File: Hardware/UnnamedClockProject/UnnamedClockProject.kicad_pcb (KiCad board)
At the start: 2 copper layers, 77.9 x 33.9 mm, 27 parts, among them J101 CLOCK_OUT, J102 POWER, Q101 2N3904, U104 G3MB-202P, U105 G3MB-202P, U106 G3MB-202P, U107 CAT24C256

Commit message: Got some work done on pcb
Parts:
- added C101: 100nF, Capacitor_THT:C_Disc_D5.0mm_W2.5mm_P5.00mm, F.Cu at (-18.0, -1.50)
- added D101: STAT_LED, LED_THT:LED_D5.0mm, F.Cu at (33.0, 5.72)
- added D102: PWR, LED_THT:LED_D5.0mm, F.Cu at (26.0, 5.75)
- added R112: 1k, Resistor_THT:R_Axial_DIN0207_L6.3mm_D2.5mm_P10.16mm_Horizontal, F.Cu at (43.5, 22.6)
- added R113: 1k, Resistor_THT:R_Axial_DIN0207_L6.3mm_D2.5mm_P10.16mm_Horizontal, F.Cu at (40.0, 22.6)
- added REF**: OSHW-Logo2_14.6x12mm_SilkScreen, Symbol:OSHW-Logo2_14.6x12mm_SilkScreen, F.Cu at (-80.0, -27.0)
- added REF**: KiCad-Logo2_12mm_SilkScreen, Symbol:KiCad-Logo2_12mm_SilkScreen, B.Cu at (7.00, 50.0)
- added REF**: OSHW-Logo2_14.6x12mm_SilkScreen, Symbol:OSHW-Logo2_14.6x12mm_SilkScreen, B.Cu at (8.00, 36.0)
- RV101: footprint Potentiometer_THT:Potentiometer_Bourns_3339S_Horizontal -> Potentiometer_THT:Potentiometer_Runtron_RM-065_Vertical
- U108: moved to B.Cu
- moved RV101 374.8 mm to (-16.5, -15.8), turned to 180 degrees
- moved U107 363.7 mm to (-21.5, -8.50), turned to -90 degrees
- moved U103 335.5 mm to (-18.0, 37.0), turned to -90 degrees
- moved R111 329.1 mm to (-50.0, -30.0)
- moved Q101 306.2 mm to (34.5, 41.5), turned to 90 degrees
- moved R102 284.1 mm to (-37.7, 33.0)
- moved R101 282.8 mm to (-37.7, 36.5)
- moved D106 250.2 mm to (47.0, 5.72), turned to -90 degrees
- moved D105 237.7 mm to (54.0, 5.72), turned to -90 degrees
- moved D103 236.8 mm to (40.0, 5.72), turned to -90 degrees
- moved U104 233.3 mm to (38.4, 27.3)
- moved J102 232.7 mm to (30.9, 50.5)
- moved R105 231.1 mm to (19.5, 34.0)
- moved R104 231.0 mm to (19.4, 30.5)
- moved U106 229.5 mm to (43.4, 39.3)
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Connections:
- A101 pad 28: unconnected-(A101-D13-Pad28) -> /STAT
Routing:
- net /24VAC_L: track 0.00 -> 41.8 mm
- net /L1_OUT: track 0.00 -> 20.0 mm
- net Net-(U104-Pad14): track 0.00 -> 12.0 mm
- net /L2_OUT: track 0.00 -> 11.9 mm
- net /24VAC_N: track 0.00 -> 10.6 mm
- added copper zone on B.Cu, net GND
- added copper zone on F.Cu, net GND
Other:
- board size 77.9 x 33.9 mm -> 160 x 102 mm
- board text added: "!DIR"
- board text added: "24N"
- board text added: "24VAC"
- board text added: "CLOCK_OUT"
- board text added: "CONTRAST"
- board text added: "DIR"
- board text added: "FIX"
- board text added: "L1"
- board text added: "L2"
- board text added: "MOVE"
- board text added: "POWER"
- board text added: "PWR"
- board text added: "STAT"

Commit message: Knock out a little more before class
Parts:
- added J103: BUTTONS, Connector_JST:JST_EH_B6B-EH-A_1x06_P2.50mm_Vertical, F.Cu at (18.5, 19.0)
- moved U103 11.5 mm to (-18.0, 48.5)
- moved R101 11.0 mm to (-37.6, 47.5)
- moved R102 11.0 mm to (-37.6, 44.0)
- moved REF** 3.75 mm to (10.0, 47.8)
- moved REF** 2.06 mm to (10.0, 35.5)
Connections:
- A101 pad 10: unconnected-(A101-A1-Pad10) -> /DN_BTN
- A101 pad 11: unconnected-(A101-A2-Pad11) -> /LF_BTN
- A101 pad 12: unconnected-(A101-A3-Pad12) -> /RI_BTN
- A101 pad 15: unconnected-(A101-D0/RX-Pad15) -> /MENU_BTN
- A101 pad 9: unconnected-(A101-A0-Pad9) -> /UP_BTN
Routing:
- net +5V: track 0.00 -> 268.6 mm
- net /REG_SEL: track 0.00 -> 101.1 mm
- net /LCD_EN: track 0.00 -> 99.0 mm
- net /LCD_7: track 0.00 -> 88.9 mm
- net /LCD_6: track 0.00 -> 88.9 mm
- net /LCD_5: track 0.00 -> 88.9 mm
- net /LCD_4: track 0.00 -> 88.9 mm
- net /DIR: track 0.00 -> 42.8 mm
- net /NOT_DIR: track 0.00 -> 41.1 mm
- net /EN: track 0.00 -> 36.6 mm
- net Net-(U108-CONTRAST): track 0.00 -> 17.8 mm
- net Net-(D102-A): track 0.00 -> 15.7 mm
- net Net-(R105-Pad2): track 0.00 -> 15.2 mm
- net Net-(D101-A): track 0.00 -> 12.2 mm
- net Net-(R104-Pad2): track 0.00 -> 10.1 mm
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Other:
- outline, holes or cut-outs redrawn

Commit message: Complete mounting
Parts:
- moved U103 2.75 mm to (-18.0, 45.8)
- moved U107 1.77 mm to (-21.7, -10.2)
- moved C101 1.35 mm to (-18.5, -2.75)
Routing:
- net /STAT: track 0.00 -> 146.4 mm
- net /RI_BTN: track 0.00 -> 122.9 mm, vias 0 -> 2
- net /SDA: track 0.00 -> 120.5 mm, vias 0 -> 2
- net /SCL: track 0.00 -> 118.6 mm, vias 0 -> 2
- net /DIR: track 42.8 -> 153.8 mm, vias 0 -> 3
- net /EN: track 36.6 -> 145.5 mm, vias 0 -> 3
- net /MENU_BTN: track 0.00 -> 103.7 mm, vias 0 -> 3
- net /GPS_TX: track 0.00 -> 102.7 mm, vias 0 -> 2
- net /GPS_RX: track 0.00 -> 97.0 mm, vias 0 -> 4
- net Net-(U102-FIX): track 0.00 -> 74.1 mm
- net /GPS_PPS: track 0.00 -> 68.7 mm, vias 0 -> 3
- net /UP_BTN: track 0.00 -> 62.7 mm
- net /DN_BTN: track 0.00 -> 60.6 mm
- net /LF_BTN: track 0.00 -> 58.4 mm
- net /LCD_EN: track 99.0 -> 147.6 mm, vias 0 -> 1
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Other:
- board text added: "Unnamed Clock Project AC1JA ${FULL_REVISION}"

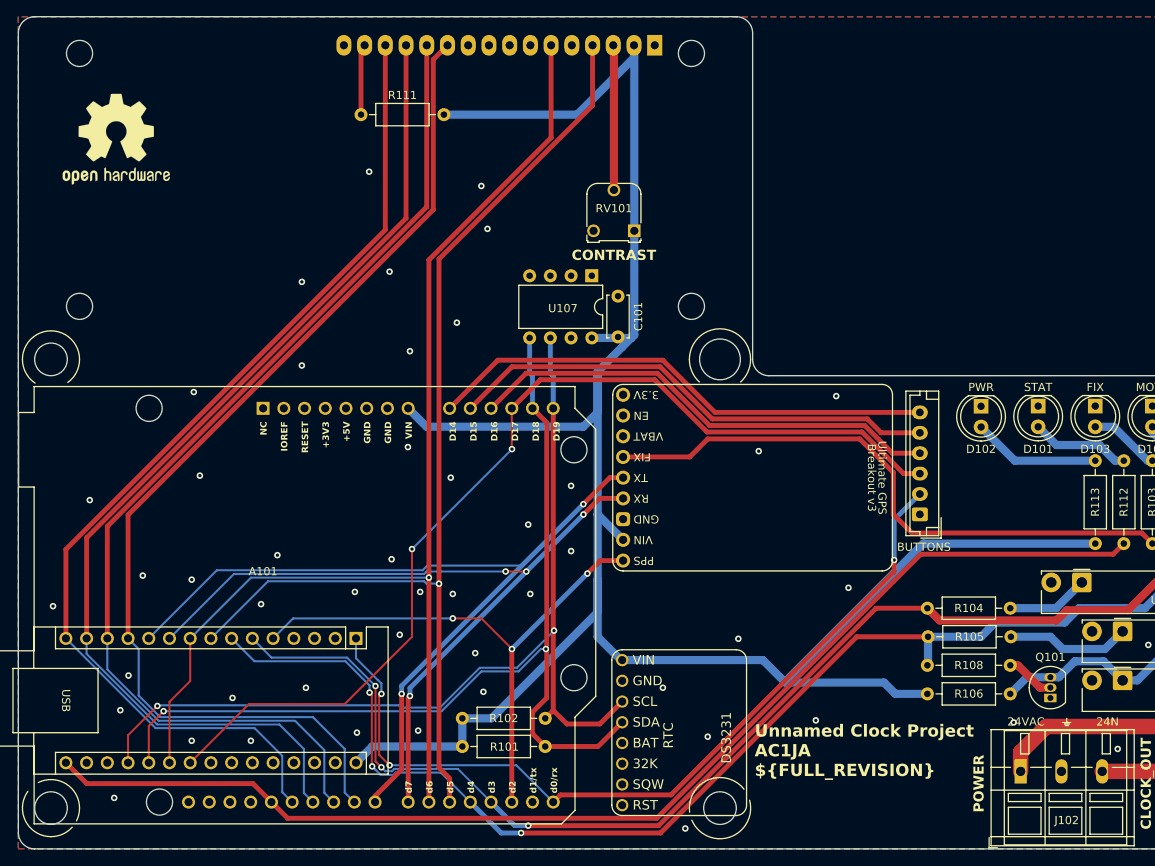
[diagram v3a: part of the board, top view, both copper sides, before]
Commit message: Add amazon dro from upstream, fix logos and prep for RC2
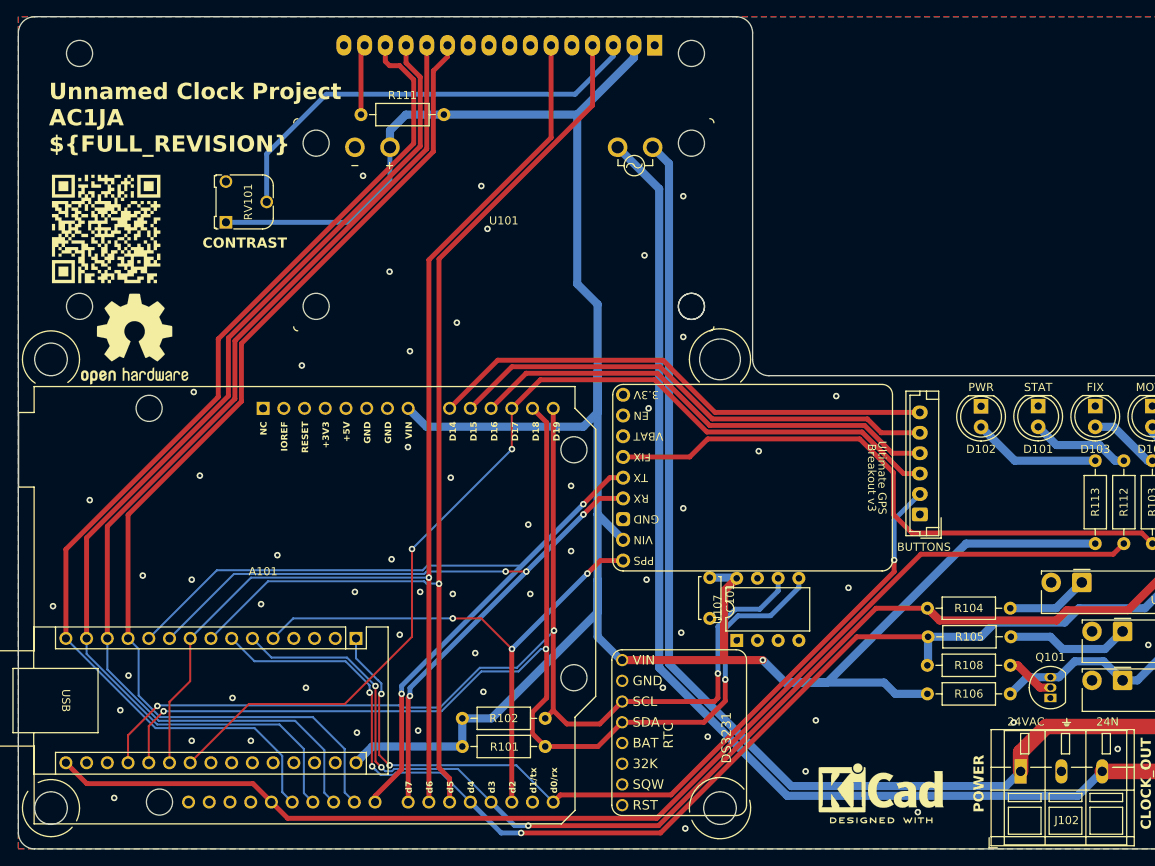
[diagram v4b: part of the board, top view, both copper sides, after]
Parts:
- removed the REF** at (10.0, 47.8)
- removed the REF** at (10.0, 35.5)
- added G***: LOGO, Project:tag_0.1, F.Cu at (-81.2, -16.0)
- added REF**: KiCad-Logo2_6mm_SilkScreen, Symbol:KiCad-Logo2_6mm_SilkScreen, F.Cu at (13.8, 52.5)
- added REF**: KiCad-Logo2_6mm_SilkScreen, Symbol:KiCad-Logo2_6mm_SilkScreen, B.Cu at (13.8, 52.5)
- added U101: ~, ac1ja:Amazon_DRO, F.Cu at (-32.5, -16.5)
- moved RV101 50.1 mm to (-66.6, -16.8), turned to 90 degrees
- moved U107 48.1 mm to (-3.95, 34.5), turned to 90 degrees
- moved C101 31.6 mm to (-7.25, 26.8), turned to -90 degrees
- moved REF** 24.6 mm to (-77.8, -2.50)
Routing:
- net /24VAC_N: track 10.6 -> 138.6 mm
- net /24VAC_L: track 41.8 -> 156.0 mm
- net Net-(U108-CONTRAST): track 17.8 -> 54.8 mm
- net +5V: track 273.4 -> 308.4 mm, vias 0 -> 1
- net /SDA: track 120.5 -> 146.6 mm, vias 2 -> 3
- net /SCL: track 118.6 -> 141.2 mm, vias 2 -> 3
- net /LCD_7: track 127.6 -> 131.2 mm
- net /LCD_6: track 129.2 -> 130.7 mm
- net GND: vias 53 -> 61
